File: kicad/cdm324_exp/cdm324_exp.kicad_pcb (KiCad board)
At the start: 2 copper layers, 60 x 17.6 mm, 29 parts, among them J1 Conn_02x04_Odd_Even, J2 Conn_02x04_Odd_Even, J3 USB_C_Receptacle_USB2.0, J5 Micro_SD_Card_Det1, J6 Conn_01x04_Socket, J7 AudioJack4, SW1 SW_Push, SW2 SW_Push, SW3 SW_DIP_x01, U1 CH340X

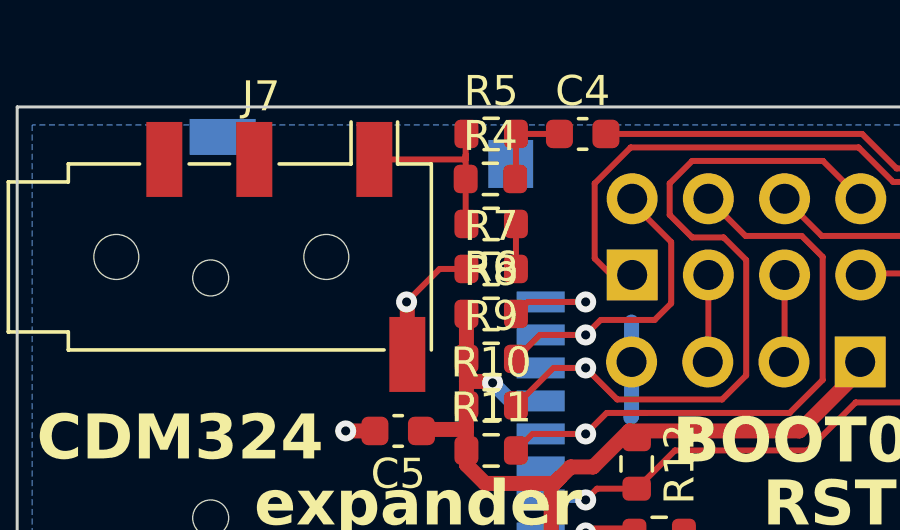
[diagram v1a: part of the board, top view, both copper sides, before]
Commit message: correct resistor divider for jack output
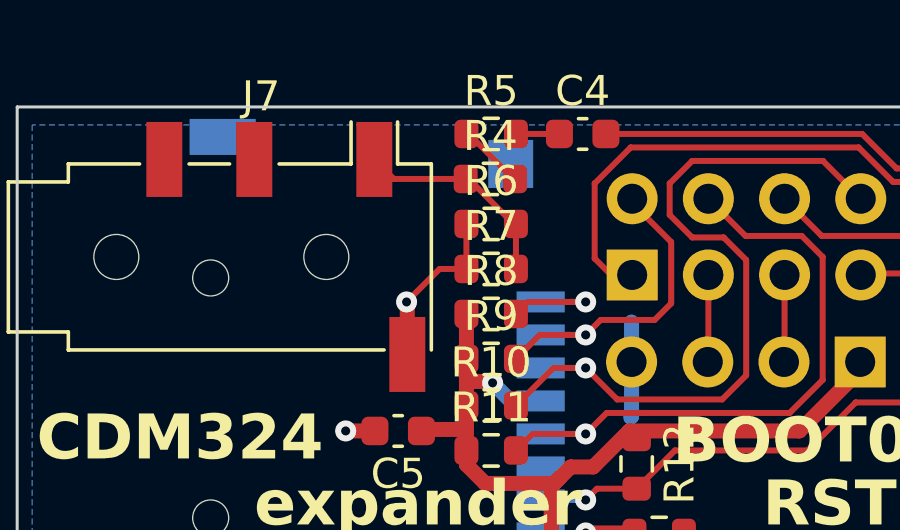
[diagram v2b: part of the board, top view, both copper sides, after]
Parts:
- turned R6 to 0 degrees
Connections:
- R4 pad 2: Net-(C4-Pad1) -> Net-(R4-Pad2)
- R5 pad 1: Net-(J7-PadT) -> Net-(R4-Pad2)
- R6 pad 1: Net-(R6-Pad1) -> GND
- R7 pad 2: Net-(R6-Pad1) -> Net-(J7-PadT)
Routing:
- net Net-(R4-Pad2): track 0.00 -> 2.32 mm
- net Net-(C4-Pad1): track 2.96 -> 1.45 mm
- net Net-(R6-Pad1): track 1.50 -> 0.00 mm
- net GND: track 25.3 -> 26.8 mm
- net Net-(J7-PadT): track 6.69 -> 7.59 mm
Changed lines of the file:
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@@
   (net 25 "unconnected-(J3-SBU1-PadA8)")
   (net 26 "Net-(U1-~{RTS})")
-  (net 27 "Net-(R6-Pad1)")
+  (net 27 "Net-(R4-Pad2)")
   (net 28 "Net-(J5-DAT2)")
   (net 29 "Net-(J5-DAT1)")
@@
       (net 33 "Net-(J7-PadT)") (pintype "passive"))
     (pad "2" smd roundrect (at 0.825 0) (size 0.8 0.95) (layers "F.Cu" "F.Paste" "F.Mask") (roundrect_rratio 0.25)
-      (net 5 "Net-(C4-Pad1)") (pintype "passive"))
+      (net 27 "Net-(R4-Pad2)") (pintype "passive"))
     (model "${KICAD6_3DMODEL_DIR}/Resistor_SMD.3dshapes/R_0603_1608Metric.wrl"
       (offset (xyz 0 0 0))
@@
       (stroke (width 0.1) (type solid)) (layer "F.Fab"))
     (pad "1" smd roundrect (at -0.825 0) (size 0.8 0.95) (layers "F.Cu" "F.Paste" "F.Mask") (roundrect_rratio 0.25)
-      (net 33 "Net-(J7-PadT)") (pintype "passive"))
+      (net 27 "Net-(R4-Pad2)") (pintype "passive"))
     (pad "2" smd roundrect (at 0.825 0) (size 0.8 0.95) (layers "F.Cu" "F.Paste" "F.Mask") (roundrect_rratio 0.25)
       (net 5 "Net-(C4-Pad1)") (pintype "passive"))
@@
     (descr "Resistor SMD 0603 (1608 Metric), square (rectangular) end terminal, IPC_7351 nominal, (Body size source: IPC-SM-782 page 72, https://www.pcb-3d.com/wordpress/wp-content/uploads/ipc-sm-782a_amendment_1_and_2.pdf), generated with kicad-footprint-generator")
     (tags "resistor")
+    (property "Field4" "C114624")
     (property "Sheetfile" "cdm324_exp.kicad_sch")
     (property "Sheetname" "")
@@
     (descr "Resistor SMD 0603 (1608 Metric), square (rectangular) end terminal, IPC_7351 nominal, (Body size source: IPC-SM-782 page 72, https://www.pcb-3d.com/wordpress/wp-content/uploads/ipc-sm-782a_amendment_1_and_2.pdf), generated with kicad-footprint-generator")
     (tags "resistor")
+    (property "Field4" "C114624")
     (property "Sheetfile" "cdm324_exp.kicad_sch")
     (property "Sheetname" "")
@@
     (descr "Resistor SMD 0603 (1608 Metric), square (rectangular) end terminal, IPC_7351 nominal, (Body size source: IPC-SM-782 page 72, https://www.pcb-3d.com/wordpress/wp-content/uploads/ipc-sm-782a_amendment_1_and_2.pdf), generated with kicad-footprint-generator")
     (tags "resistor")
+    (property "Field4" "C114624")
     (property "Sheetfile" "cdm324_exp.kicad_sch")
     (property "Sheetname" "")
@@
     (descr "Resistor SMD 0603 (1608 Metric), square (rectangular) end terminal, IPC_7351 nominal, (Body size source: IPC-SM-782 page 72, https://www.pcb-3d.com/wordpress/wp-content/uploads/ipc-sm-782a_amendment_1_and_2.pdf), generated with kicad-footprint-generator")
     (tags "resistor")
+    (property "Field4" "C114624")
     (property "Sheetfile" "cdm324_exp.kicad_sch")
     (property "Sheetname" "")
@@
     (descr "Resistor SMD 0603 (1608 Metric), square (rectangular) end terminal, IPC_7351 nominal, (Body size source: IPC-SM-782 page 72, https://www.pcb-3d.com/wordpress/wp-content/uploads/ipc-sm-782a_amendment_1_and_2.pdf), generated with kicad-footprint-generator")
     (tags "resistor")
+    (property "Field4" "C114624")
     (property "Sheetfile" "cdm324_exp.kicad_sch")
     (property "Sheetname" "")
@@
     (descr "Resistor SMD 0603 (1608 Metric), square (rectangular) end terminal, IPC_7351 nominal, (Body size source: IPC-SM-782 page 72, https://www.pcb-3d.com/wordpress/wp-content/uploads/ipc-sm-782a_amendment_1_and_2.pdf), generated with kicad-footprint-generator")
     (tags "resistor")
+    (property "Field4" "C114624")
     (property "Sheetfile" "cdm324_exp.kicad_sch")
     (property "Sheetname" "")
@@
       (net 2 "GND") (pintype "passive"))
     (pad "2" smd roundrect (at 0.825 0) (size 0.8 0.95) (layers "F.Cu" "F.Paste" "F.Mask") (roundrect_rratio 0.25)
-      (net 27 "Net-(R6-Pad1)") (pintype "passive"))
+      (net 33 "Net-(J7-PadT)") (pintype "passive"))
     (model "${KICAD6_3DMODEL_DIR}/Resistor_SMD.3dshapes/R_0603_1608Metric.wrl"
       (offset (xyz 0 0 0))
@@
   )
   (footprint "Resistor_SMD:R_0603_1608Metric" (layer "F.Cu")
-    (at 95.3 98.3 180)
+    (at 95.3 98.3)
     (descr "Resistor SMD 0603 (1608 Metric), square (rectangular) end terminal, IPC_7351 nominal, (Body size source: IPC-SM-782 page 72, https://www.pcb-3d.com/wordpress/wp-content/uploads/ipc-sm-782a_amendment_1_and_2.pdf), generated with kicad-footprint-generator")
     (tags "resistor")
@@
     (fp_line (start 0.8 0.4125) (end -0.8 0.4125)
       (stroke (width 0.1) (type solid)) (layer "F.Fab"))
-    (pad "1" smd roundrect (at -0.825 0 180) (size 0.8 0.95) (layers "F.Cu" "F.Paste" "F.Mask") (roundrect_rratio 0.25)
-      (net 27 "Net-(R6-Pad1)") (pintype "passive"))
-    (pad "2" smd roundrect (at 0.825 0 180) (size 0.8 0.95) (layers "F.Cu" "F.Paste" "F.Mask") (roundrect_rratio 0.25)
+    (pad "1" smd roundrect (at -0.825 0) (size 0.8 0.95) (layers "F.Cu" "F.Paste" "F.Mask") (roundrect_rratio 0.25)
+      (net 2 "GND") (pintype "passive"))
+    (pad "2" smd roundrect (at 0.825 0) (size 0.8 0.95) (layers "F.Cu" "F.Paste" "F.Mask") (roundrect_rratio 0.25)
       (net 33 "Net-(J7-PadT)") (pintype "passive"))
     (model "${KICAD6_3DMODEL_DIR}/Resistor_SMD.3dshapes/R_0603_1608Metric.wrl"
@@
   (segment (start 129.775 98.75) (end 128.85 98.75) (width 0.5) (layer "F.Cu") (net 2))
   (segment (start 127.9 103) (end 127.05 103) (width 0.3) (layer "F.Cu") (net 2))
+  (segment (start 94.475 99.8) (end 94.475 98.3) (width 0.2) (layer "F.Cu") (net 2))
   (segment (start 133.275 103.2) (end 133.275 103.72) (width 0.5) (layer "F.Cu") (net 2))
   (segment (start 92.505 102.65) (end 92.505 100.925) (width 0.5) (layer "F.Cu") (net 2))
@@
   (segment (start 123.5 102.5) (end 121.675 102.5) (width 0.3) (layer "F.Cu") (net 4))
   (segment (start 129.8125 95.7) (end 129.08 95.7) (width 0.5) (layer "F.Cu") (net 4))
-  (segment (start 96.125 96.775) (end 96.1 96.8) (width 0.2) (layer "F.Cu") (net 5))
   (segment (start 97.575 95.3) (end 96.125 95.3) (width 0.2) (layer "F.Cu") (net 5))
-  (segment (start 96.125 95.3) (end 96.125 96.775) (width 0.2) (layer "F.Cu") (net 5))
   (segment (start 99.375 95.3) (end 99.25 95.3) (width 0.2) (layer "F.Cu") (net 6))
   (segment (start 108.815686 96.45) (end 107.665686 95.3) (width 0.2) (layer "F.Cu") (net 6))
@@
   (segment (start 126.55 102.5) (end 125.65 103.4) (width 0.2) (layer "F.Cu") (net 26))
   (segment (start 122.7 109.15) (end 120.25 109.15) (width 0.2) (layer "F.Cu") (net 26))
-  (segment (start 96.125 98.3) (end 96.125 99.8) (width 0.2) (layer "F.Cu") (net 27))
+  (segment (start 96.05 96.8) (end 96.1 96.8) (width 0.2) (layer "F.Cu") (net 27))
+  (segment (start 94.55 95.3) (end 96.05 96.8) (width 0.2) (layer "F.Cu") (net 27))
+  (segment (start 94.475 95.3) (end 94.55 95.3) (width 0.2) (layer "F.Cu") (net 27))
+  (segment (start 96.125 96.775) (end 96.1 96.8) (width 0.2) (layer "F.Cu") (net 27))
+  (segment (start 94.45 95.325) (end 94.475 95.3) (width 0.2) (layer "F.Cu") (net 27))
   (segment (start 98.45 100.9) (end 96.525 100.9) (width 0.2) (layer "F.Cu") (net 28))
   (segment (start 96.125 101.3) (end 96.05 101.3) (width 0.2) (layer "F.Cu") (net 28))
@@
   (via (at 98.45 108.6) (size 0.7) (drill 0.3) (layers "F.Cu" "B.Cu") (net 29))
   (segment (start 96.95 108.6) (end 98.45 108.6) (width 0.2) (layer "B.Cu") (net 29))
-  (segment (start 94.45 96.8) (end 94.45 96) (width 0.2) (layer "F.Cu") (net 33))
-  (segment (start 94.45 96.8) (end 94.45 98.275) (width 0.2) (layer "F.Cu") (net 33))
-  (segment (start 94.45 96) (end 94.45 96.15) (width 0.2) (layer "F.Cu") (net 33))
+  (segment (start 94.55 96.8) (end 96.05 98.3) (width 0.2) (layer "F.Cu") (net 33))
+  (segment (start 92.05 96.8) (end 92.05 96.795) (width 0.2) (layer "F.Cu") (net 33))
   (segment (start 90.93 96.15) (end 91.405 96.15) (width 0.2) (layer "F.Cu") (net 33))
-  (segment (start 94.45 98.275) (end 94.475 98.3) (width 0.2) (layer "F.Cu") (net 33))
-  (segment (start 94.45 95.325) (end 94.475 95.3) (width 0.2) (layer "F.Cu") (net 33))
-  (segment (start 94.45 96) (end 94.45 95.325) (width 0.2) (layer "F.Cu") (net 33))
-  (segment (start 94.45 96.15) (end 91.405 96.15) (width 0.2) (layer "F.Cu") (net 33))
+  (segment (start 96.05 98.3) (end 96.125 98.3) (width 0.2) (layer "F.Cu") (net 33))
+  (segment (start 92.05 96.795) (end 91.405 96.15) (width 0.2) (layer "F.Cu") (net 33))
+  (segment (start 96.125 98.3) (end 96.125 99.8) (width 0.2) (layer "F.Cu") (net 33))
+  (segment (start 94.45 96.8) (end 94.55 96.8) (width 0.2) (layer "F.Cu") (net 33))
+  (segment (start 94.45 96.8) (end 92.05 96.8) (width 0.2) (layer "F.Cu") (net 33))
   (zone (net 2) (net_name "GND") (layer "B.Cu") (hatch edge 0.5)
     (connect_pads (clearance 0.2))
